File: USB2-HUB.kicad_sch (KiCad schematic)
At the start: 26 parts, among them J1 SM04B-GHS-TB(LF)(SN)-, J2 USB_C_Receptacle, J3 SM04B-GHS-TB(LF)(SN)-, U1 FSUSB42MUX, U2 USB2514B-I/M2, U3 TPD4EUSB30, Y1 ECS-240-18-33-JGN-TR

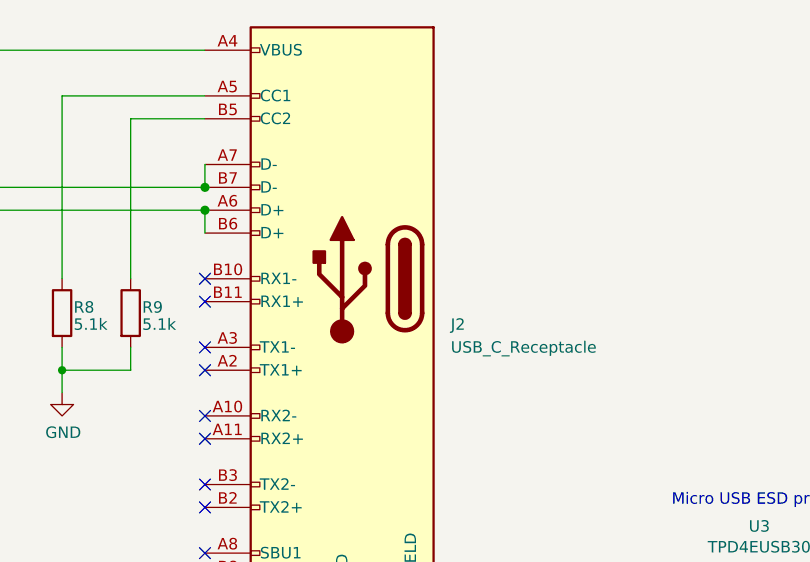
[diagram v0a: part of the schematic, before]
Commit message: added components for new DC/DC regulator
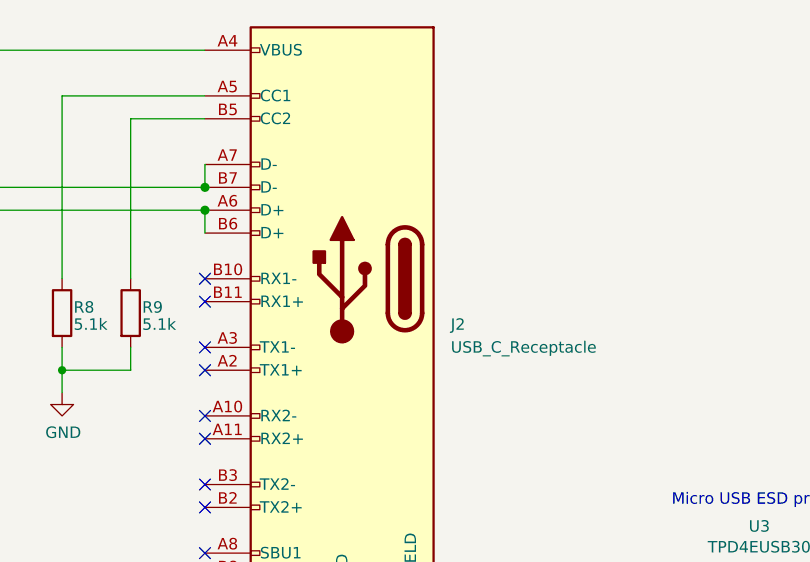
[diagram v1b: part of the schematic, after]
